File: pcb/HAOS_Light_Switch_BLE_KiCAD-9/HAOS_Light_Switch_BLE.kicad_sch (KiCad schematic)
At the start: 34 parts, among them J1 GPIO, J2 GPIO, J3 GPIO, J4 Battery_CR2032, J7 SWD, SW1 SW_Push, SW2 SW_Push, SW3 SW_Push, U1 nrf52832, U3 RF_Antenna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

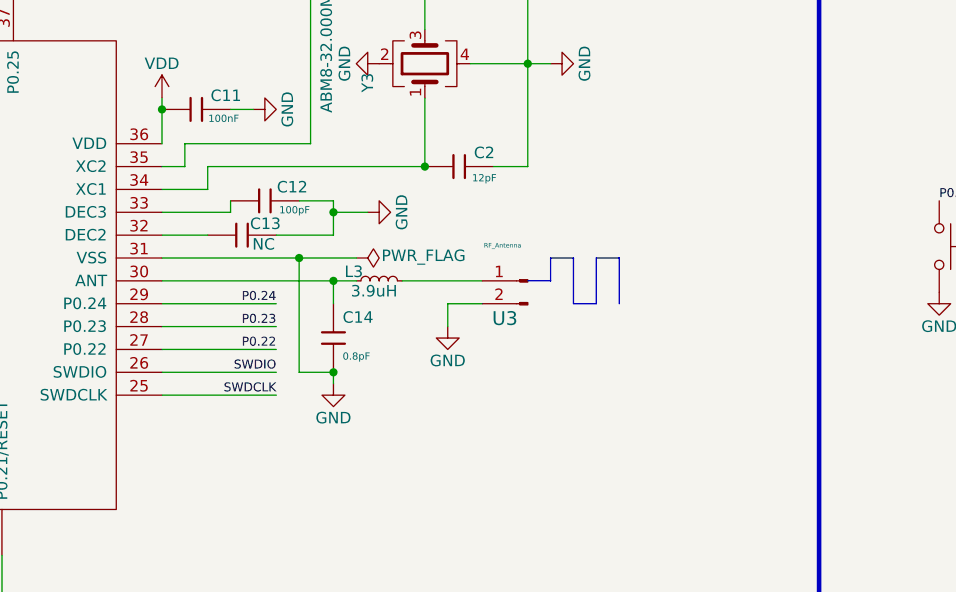
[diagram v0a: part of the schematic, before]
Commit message: Updated antenna
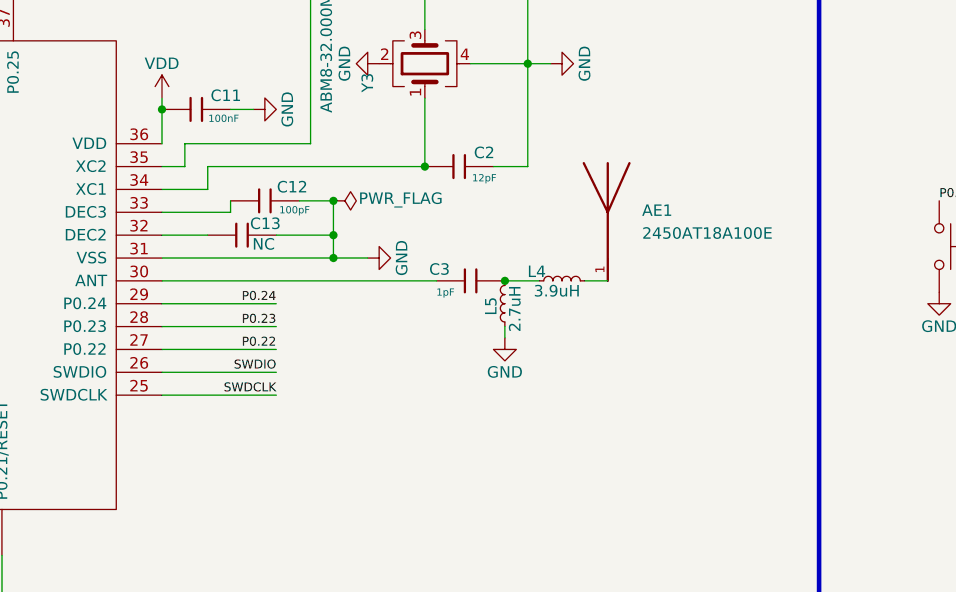
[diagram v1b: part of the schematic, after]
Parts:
- removed C14: 0.8pF, PCM_JLCPCB:C_0402, symbol PCM_JLCPCB-Capacitors:0402,1pF
- removed L3: 3.9uH, Inductor_SMD:L_0402_1005Metric_Pad0.77x0.64mm_HandSolder, symbol Device:L_Small
- removed U3: RF_Antenna, Footprints:Antenna-2.45GHZ_mirror, symbol Connector:Conn_01x02_Pin
- added AE1: 2450AT18A100E, Footprints:ANTC3216X140N, symbol BLE-Ant:2450AT18A100E
- added C3: 1pF, PCM_JLCPCB:C_0402, symbol PCM_JLCPCB-Capacitors:0402,1pF
- added L4: 3.9uH, Inductor_SMD:L_0402_1005Metric_Pad0.77x0.64mm_HandSolder, symbol Device:L_Small
- added L5: 2.7uH, Inductor_SMD:L_0402_1005Metric_Pad0.77x0.64mm_HandSolder, symbol Device:L_Small
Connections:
- net GND: now also L5.1
- net at U1.30 (ANT): now also C3.1
- new net: C3.2, L4.1, L5.2
- new net: AE1.1, L4.2

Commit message: Potential 1st spin.
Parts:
- added J5: PWR, Connector_PinHeader_1.00mm:PinHeader_1x02_P1.00mm_Vertical, symbol Connector_Generic:Conn_01x02
- C3: Capacitance 0.8pF -> 1pF; LCSC C88918 -> C1550; Manufacturer FH(Guangdong Fenghua Advanced Tech) -> (none); Part 0402CG1R0C500NT -> (none); Temperature Coefficient C0H -> COG
- Y3: LCSC C1986787 -> C1986513
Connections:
- net GND: now also J5.1 (Pin_1)
- net VDD: now also J5.2 (Pin_2)
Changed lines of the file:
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@@
 	(wire
 		(pts
+			(xy 110.49 45.72) (xy 105.41 45.72)
+		)
+		(stroke
+			(width 0)
+			(type default)
+		)
+	)
+	(wire
+		(pts
 			(xy 27.94 107.95) (xy 27.94 113.03)
 		)
@@
 	(wire
 		(pts
+			(xy 110.49 48.26) (xy 105.41 48.26)
+		)
+		(stroke
+			(width 0)
+			(type default)
+		)
+	)
+	(wire
+		(pts
 			(xy 53.34 43.18) (xy 48.26 43.18)
 		)
@@
 	(wire
 		(pts
+			(xy 105.41 48.26) (xy 105.41 49.53)
+		)
+		(stroke
+			(width 0)
+			(type default)
+		)
+	)
+	(wire
+		(pts
 			(xy 133.35 106.68) (xy 130.81 106.68)
 		)
@@
 	)
 	(symbol
+		(lib_id "Connector_Generic:Conn_01x02")
+		(at 115.57 48.26 0)
+		(mirror x)
+		(unit 1)
+		(exclude_from_sim no)
+		(in_bom yes)
+		(on_board yes)
+		(dnp no)
+		(property "Reference" "J5"
+			(at 115.57 51.054 0)
+			(effects
+				(font
+					(size 1.27 1.27)
+				)
+			)
+		)
+		(property "Value" "PWR"
+			(at 115.57 42.926 0)
+			(effects
+				(font
+					(size 1.27 1.27)
+				)
+			)
+		)
+		(property "Footprint" "Connector_PinHeader_1.00mm:PinHeader_1x02_P1.00mm_Vertical"
+			(at 115.57 48.26 0)
+			(effects
+				(font
+					(size 1.27 1.27)
+				)
+				(hide yes)
+			)
+		)
+		(property "Datasheet" "~"
+			(at 115.57 48.26 0)
+			(effects
+				(font
+					(size 1.27 1.27)
+				)
+				(hide yes)
+			)
+		)
+		(property "Description" "Generic connector, single row, 01x02, script generated (kicad-library-utils/schlib/autogen/connector/)"
+			(at 115.57 48.26 0)
+			(effects
+				(font
+					(size 1.27 1.27)
+				)
+				(hide yes)
+			)
+		)
+		(pin "1"
+		)
+		(pin "2"
+		)
+		(instances
+			(project "HAOS_Light_Switch_BLE"
+				(path "/7bf155d7-cf3f-4b19-a6e4-e06ff318c707"
+					(reference "J5")
+					(unit 1)
+				)
+			)
+		)
+	)
+	(symbol
 		(lib_id "PCM_JLCPCB-Resistors:0603,10Ω")
 		(at 181.61 31.75 90)
@@
 			)
 		)
-		(property "LCSC" "C88918"
+		(property "LCSC" "C1550"
 			(at 165.1 119.38 0)
 			(effects
@@
 			)
 		)
-		(property "Manufacturer" "FH(Guangdong Fenghua Advanced Tech)"
+		(property "Manufacturer" ""
 			(at 165.1 119.38 0)
 			(effects
@@
 			)
 		)
-		(property "Part" "0402CG1R0C500NT"
+		(property "Part" ""
 			(at 165.1 119.38 0)
 			(effects
@@
 			)
 		)
-		(property "Capacitance" "0.8pF"
+		(property "Capacitance" "1pF"
 			(at 165.1 119.38 0)
 			(effects
@@
 			)
 		)
-		(property "Temperature Coefficient" "C0H"
+		(property "Temperature Coefficient" "COG"
 			(at 165.1 119.38 0)
 			(effects
@@
 	)
 	(symbol
+		(lib_id "power:VDD")
+		(at 105.41 45.72 0)
+		(unit 1)
+		(exclude_from_sim no)
+		(in_bom yes)
+		(on_board yes)
+		(dnp no)
+		(property "Reference" "#PWR08"
+			(at 105.41 49.53 0)
+			(effects
+				(font
+					(size 1.27 1.27)
+				)
+				(hide yes)
+			)
+		)
+		(property "Value" "VDD"
+			(at 105.41 41.91 0)
+			(effects
+				(font
+					(size 1.27 1.27)
+				)
+			)
+		)
+		(property "Footprint" ""
+			(at 105.41 45.72 0)
+			(effects
+				(font
+					(size 1.27 1.27)
+				)
+				(hide yes)
+			)
+		)
+		(property "Datasheet" ""
+			(at 105.41 45.72 0)
+			(effects
+				(font
+					(size 1.27 1.27)
+				)
+				(hide yes)
+			)
+		)
+		(property "Description" ""
+			(at 105.41 45.72 0)
+			(effects
+				(font
+					(size 1.27 1.27)
+				)
+			)
+		)
+		(pin "1"
+		)
+		(instances
+			(project "HAOS_Light_Switch_BLE"
+				(path "/7bf155d7-cf3f-4b19-a6e4-e06ff318c707"
+					(reference "#PWR08")
+					(unit 1)
+				)
+			)
+		)
+	)
+	(symbol
 		(lib_id "PCM_JLCPCB-Capacitors:0402,100nF,(2)")
 		(at 77.47 153.67 180)
@@
 			)
 		)
-		(property "LCSC" "C1986787"
+		(property "LCSC" "C1986513"
 			(at 160.02 95.25 0)
 			(effects
@@
 					(unit 1)
 				)
+			)
+		)
+	)
+	(symbol
+		(lib_id "power:GND")
+		(at 105.41 49.53 0)
+		(unit 1)
+		(exclude_from_sim no)
+		(in_bom yes)
+		(on_board yes)
+		(dnp no)
+		(property "Reference" "#PWR07"
+			(at 105.41 55.88 0)
+			(effects
+				(font
+					(size 1.27 1.27)
+				)
+				(hide yes)
+			)
+		)
+		(property "Value" "GND"
+			(at 105.41 53.34 0)
+			(effects
+				(font
+					(size 1.27 1.27)
+				)
+			)
+		)
+		(property "Footprint" ""
+			(at 105.41 49.53 0)
+			(effects
+				(font
+					(size 1.27 1.27)
+				)
+				(hide yes)
+			)
+		)
+		(property "Datasheet" ""
+			(at 105.41 49.53 0)
+			(effects
+				(font
+					(size 1.27 1.27)
+				)
+				(hide yes)
+			)
+		)
+		(property "Description" ""
+			(at 105.41 49.53 0)
+			(effects
+				(font
+					(size 1.27 1.27)
+				)
+			)
+		)
+		(pin "1"
+		)
+		(instances
+			(project "HAOS_Light_Switch_BLE"
+				(path "/7bf155d7-cf3f-4b19-a6e4-e06ff318c707"
+					(reference "#PWR07")
+					(unit 1)
+				)

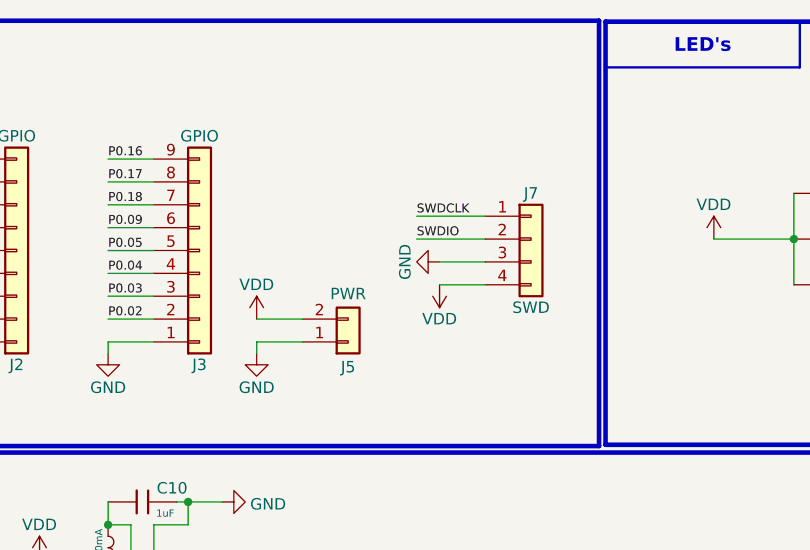
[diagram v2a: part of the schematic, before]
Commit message: added Tag-Connect programming connector
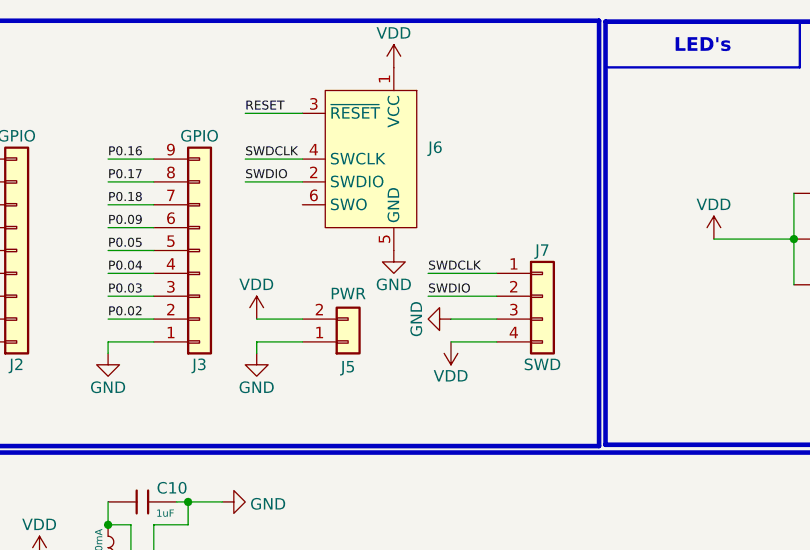
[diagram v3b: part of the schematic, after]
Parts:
- added J6: Conn_ARM_SWD_TagConnect_TC2030-NL, Connector:Tag-Connect_TC2030-IDC-NL_2x03_P1.27mm_Vertical, symbol Connector:Conn_ARM_SWD_TagConnect_TC2030-NL
- SW1, SW2, SW3: LCSC C221895 -> C2888429
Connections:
- net GND: now also J6.5 (GND)
- net RESET: now also J6.3 (~{RESET})
- net SWDCLK: now also J6.4 (SWCLK)
- net SWDIO: now also J6.2 (SWDIO)
- net VDD: now also J6.1 (VCC)
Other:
- moved on the sheet: J7

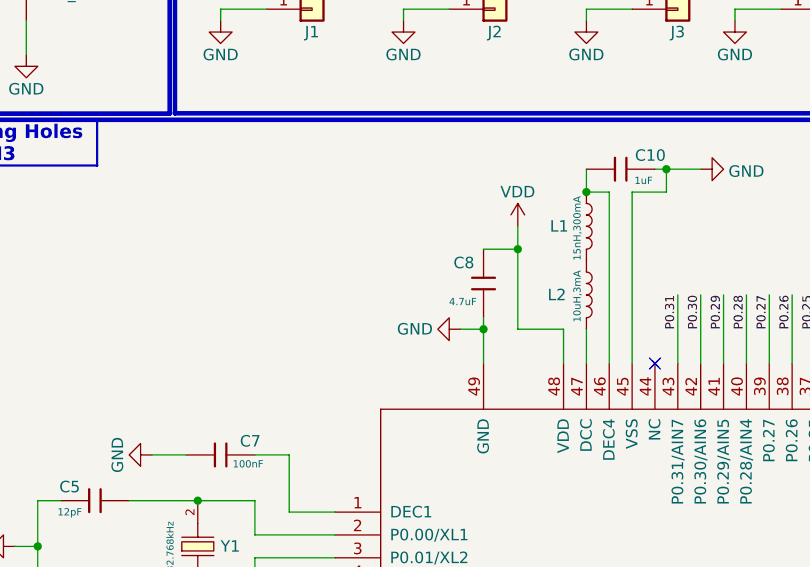
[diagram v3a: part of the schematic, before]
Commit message: Added C4 to help mitigate brown out potential during radio transmissions.
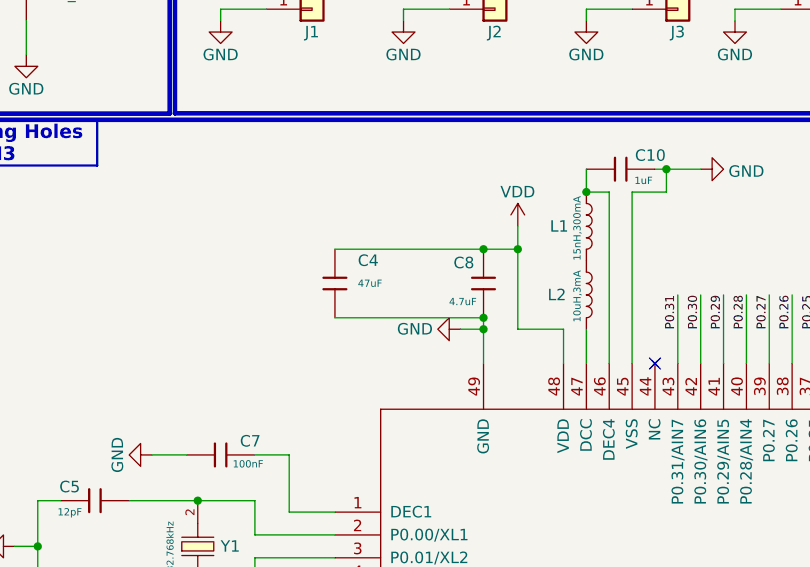
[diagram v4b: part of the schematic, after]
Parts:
- added C4: 47uF, PCM_JLCPCB:C_0805, symbol PCM_JLCPCB-Capacitors:0805,10uF
- J5: now left out of the parts list
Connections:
- net GND: now also C4.2
- net VDD: now also C4.1
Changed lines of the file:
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@@
 	)
 	(junction
+		(at 77.47 82.55)
+		(diameter 0)
+		(color 0 0 0 0)
+	)
+	(junction
 		(at 27.94 107.95)
 		(diameter 0)
@@
 	)
 	(junction
+		(at 77.47 74.93)
+		(diameter 0)
+		(color 0 0 0 0)
+	)
+	(junction
 		(at 81.28 74.93)
 		(diameter 0)
@@
 	(wire
 		(pts
+			(xy 60.96 82.55) (xy 77.47 82.55)
+		)
+		(stroke
+			(width 0)
+			(type default)
+		)
+	)
+	(wire
+		(pts
 			(xy 160.02 76.2) (xy 160.02 91.44)
 		)
@@
 		)
 	)
+	(wire
+		(pts
+			(xy 60.96 74.93) (xy 77.47 74.93)
+		)
+		(stroke
+			(width 0)
+			(type default)
+		)
+	)
 	(label "SWDIO"
 		(at 143.51 129.54 180)
@@
 		(unit 1)
 		(exclude_from_sim no)
-		(in_bom yes)
+		(in_bom no)
 		(on_board yes)
 		(dnp no)
@@
 					(unit 1)
 				)
+			)
+		)
+	)
+	(symbol
+		(lib_id "PCM_JLCPCB-Capacitors:0805,10uF")
+		(at 60.96 78.74 0)
+		(unit 1)
+		(exclude_from_sim no)
+		(in_bom yes)
+		(on_board yes)
+		(dnp no)
+		(fields_autoplaced yes)
+		(property "Reference" "C4"
+			(at 63.5 76.1999 0)
+			(effects
+				(font
+					(size 1.27 1.27)
+				)
+				(justify left)
+			)
+		)
+		(property "Value" "47uF"
+			(at 63.5 78.74 0)
+			(effects
+				(font
+					(size 0.8 0.8)
+				)
+				(justify left)
+			)
+		)
+		(property "Footprint" "PCM_JLCPCB:C_0805"
+			(at 59.182 78.74 90)
+			(effects
+				(font
+					(size 1.27 1.27)
+				)
+				(hide yes)
+			)
+		)
+		(property "Datasheet" ""
+			(at 60.96 78.74 0)
+			(effects
+				(font
+					(size 1.27 1.27)
+				)
+				(hide yes)
+			)
+		)
+		(property "Description" "10V 47uF X5R ±20% 0805 Multilayer"
+			(at 60.96 78.74 0)
+			(effects
+				(font
+					(size 1.27 1.27)
+				)
+				(hide yes)
+			)
+		)
+		(property "LCSC" "C124129"
+			(at 60.96 78.74 0)
+			(effects
+				(font
+					(size 1.27 1.27)
+				)
+				(hide yes)
+			)
+		)
+		(property "Stock" ""
+			(at 60.96 78.74 0)
+			(effects
+				(font
+					(size 1.27 1.27)
+				)
+				(hide yes)
+			)
+		)
+		(property "Price" ""
+			(at 60.96 78.74 0)
+			(effects
+				(font
+					(size 1.27 1.27)
+				)
+				(hide yes)
+			)
+		)
+		(property "Process" "SMT"
+			(at 60.96 78.74 0)
+			(effects
+				(font
+					(size 1.27 1.27)
+				)
+				(hide yes)
+			)
+		)
+		(property "Minimum Qty" "20"
+			(at 60.96 78.74 0)
+			(effects
+				(font
+					(size 1.27 1.27)
+				)
+				(hide yes)
+			)
+		)
+		(property "Attrition Qty" "10"
+			(at 60.96 78.74 0)
+			(effects
+				(font
+					(size 1.27 1.27)
+				)
+				(hide yes)
+			)
+		)
+		(property "Class" ""
+			(at 60.96 78.74 0)
+			(effects
+				(font
+					(size 1.27 1.27)
+				)
+				(hide yes)
+			)
+		)
+		(property "Category" ""
+			(at 60.96 78.74 0)
+			(effects
+				(font
+					(size 1.27 1.27)
+				)
+				(hide yes)
+			)
+		)
+		(property "Manufacturer" ""
+			(at 60.96 78.74 0)
+			(effects
+				(font
+					(size 1.27 1.27)
+				)
+				(hide yes)
+			)
+		)
+		(property "Part" ""
+			(at 60.96 78.74 0)
+			(effects
+				(font
+					(size 1.27 1.27)
+				)
+				(hide yes)
+			)
+		)
+		(property "Voltage Rated" ""
+			(at 63.5 81.28 0)
+			(effects
+				(font
+					(size 0.8 0.8)
+				)
+				(justify left)
+			)
+		)
+		(property "Tolerance" ""
+			(at 60.96 78.74 0)
+			(effects
+				(font
+					(size 1.27 1.27)
+				)
+				(hide yes)
+			)
+		)
+		(property "Capacitance" ""
+			(at 60.96 78.74 0)
+			(effects
+				(font
+					(size 1.27 1.27)
+				)
+				(hide yes)
+			)
+		)
+		(property "Temperature Coefficient" ""
+			(at 60.96 78.74 0)
+			(effects
+				(font
+					(size 1.27 1.27)
+				)
+				(hide yes)
+			)
+		)
+		(pin "2"
+		)
+		(pin "1"
+		)
+		(instances
+			(project ""
+				(path "/7bf155d7-cf3f-4b19-a6e4-e06ff318c707"
+					(reference "C4")
+					(unit 1)
+				)

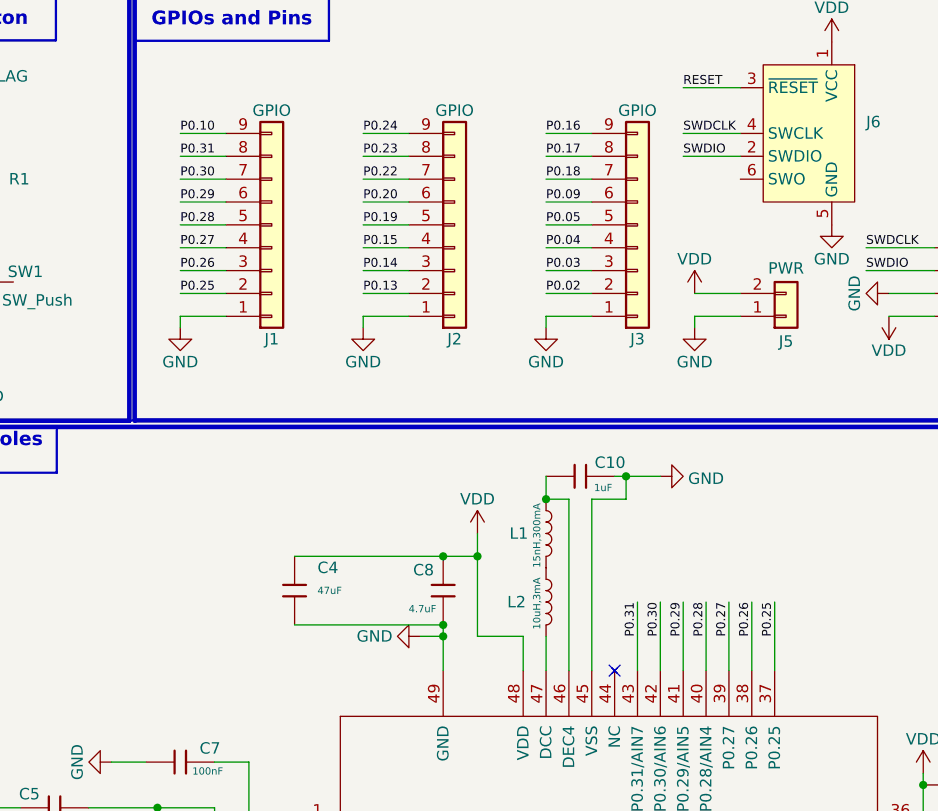
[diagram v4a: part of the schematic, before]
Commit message: Added SWO to Tag-Connect
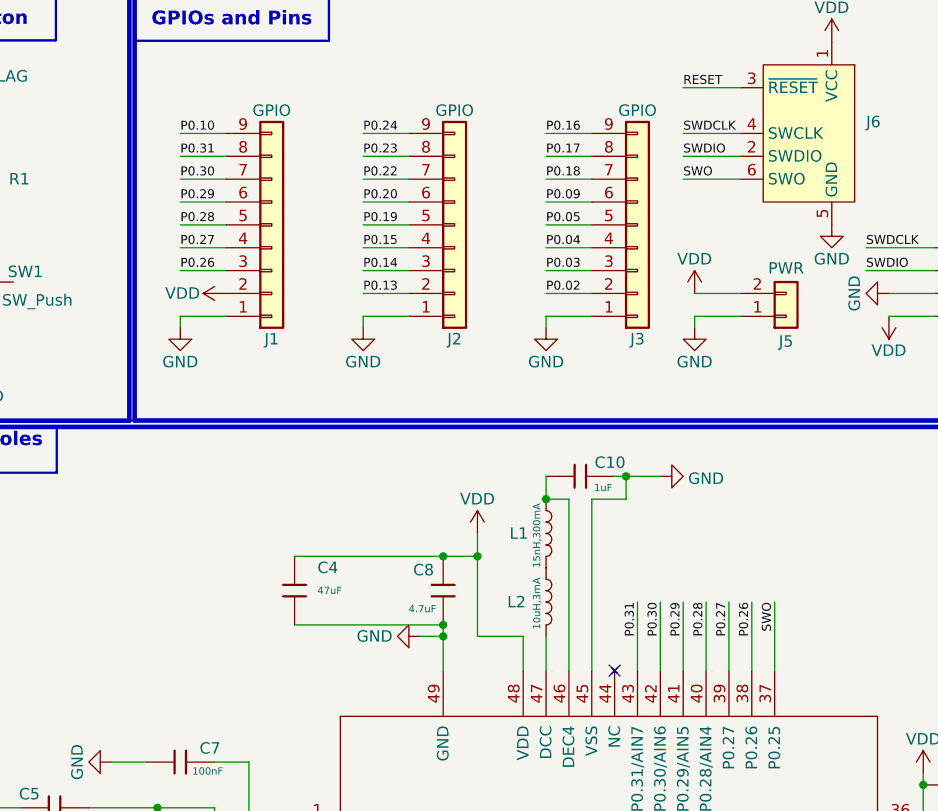
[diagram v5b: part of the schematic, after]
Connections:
- net VDD: now also J1.2 (Pin_2)
- net SWO: now reaches J6.6 (SWO)
- net SWO: now also U1.37 (P0.25)
- removed net P0.25: J1.2 (Pin_2), U1.37 (P0.25)
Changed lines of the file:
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@@
 	(wire
 		(pts
+			(xy 110.49 33.02) (xy 104.14 33.02)
+		)
+		(stroke
+			(width 0)
+			(type default)
+		)
+	)
+	(wire
+		(pts
 			(xy 149.86 116.84) (xy 153.67 116.84)
 		)
@@
 	(wire
 		(pts
-			(xy 53.34 45.72) (xy 48.26 45.72)
-		)
-		(stroke
-			(width 0)
-			(type default)
-		)
-	)
-	(wire
-		(pts
 			(xy 171.45 76.2) (xy 171.45 95.25)
 		)
@@
 		)
 	)
+	(label "SWO"
+		(at 104.14 33.02 0)
+		(effects
+			(font
+				(size 0.9906 0.9906)
+			)
+			(justify left bottom)
+		)
+	)
 	(label "P0.23"
 		(at 143.51 124.46 180)
@@
 		)
 	)
-	(label "P0.25"
+	(label "SWO"
 		(at 114.3 80.01 270)
 		(effects
@@
 		)
 	)
-	(label "P0.25"
-		(at 48.26 45.72 0)
-		(effects
-			(font
-				(size 0.9906 0.9906)
-			)
-			(justify left bottom)
-		)
-	)
 	(label "SWDCLK"
 		(at 124.46 40.64 0)
@@
 					(unit 1)
 				)
+			)
+		)
+	)
+	(symbol
+		(lib_id "power:VDD")
+		(at 53.34 45.72 90)
+		(unit 1)
+		(exclude_from_sim no)
+		(in_bom yes)
+		(on_board yes)
+		(dnp no)
+		(property "Reference" "#PWR030"
+			(at 57.15 45.72 0)
+			(effects
+				(font
+					(size 1.27 1.27)
+				)
+				(hide yes)
+			)
+		)
+		(property "Value" "VDD"
+			(at 48.514 45.72 90)
+			(effects
+				(font
+					(size 1.27 1.27)
+				)
+			)
+		)
+		(property "Footprint" ""
+			(at 53.34 45.72 0)
+			(effects
+				(font
+					(size 1.27 1.27)
+				)
+				(hide yes)
+			)
+		)
+		(property "Datasheet" ""
+			(at 53.34 45.72 0)
+			(effects
+				(font
+					(size 1.27 1.27)
+				)
+				(hide yes)
+			)
+		)
+		(property "Description" ""
+			(at 53.34 45.72 0)
+			(effects
+				(font
+					(size 1.27 1.27)
+				)
+			)
+		)
+		(pin "1"
+		)
+		(instances
+			(project "HAOS_Light_Switch_BLE"
+				(path "/7bf155d7-cf3f-4b19-a6e4-e06ff318c707"
+					(reference "#PWR030")
+					(unit 1)
+				)
